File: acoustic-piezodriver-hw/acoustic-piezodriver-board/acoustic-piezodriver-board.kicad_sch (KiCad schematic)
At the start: 0 parts

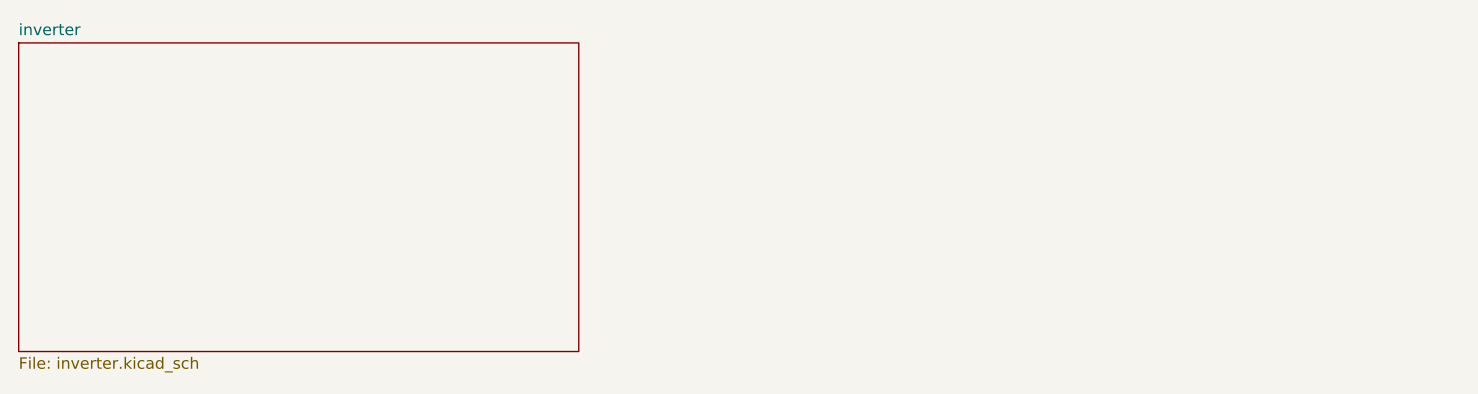
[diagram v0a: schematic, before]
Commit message: [carrier] Same as previous [piezodriver] Moved inverter to separate board
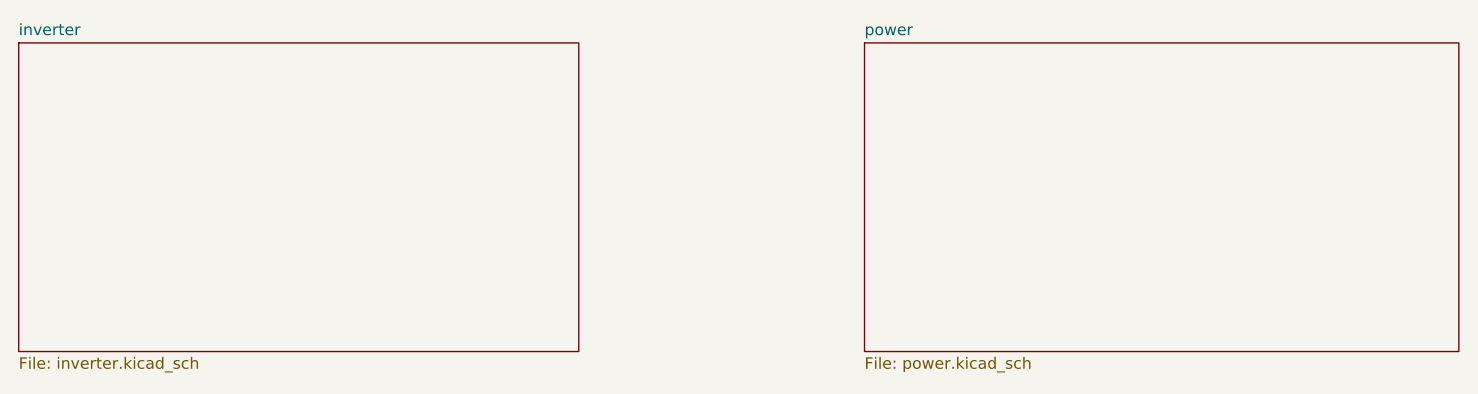
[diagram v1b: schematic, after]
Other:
- added sheet power (power.kicad_sch)
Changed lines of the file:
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@@
+		)
+	)
+	(sheet
+		(at 129.54 41.91)
+		(size 66.04 34.29)
+		(exclude_from_sim no)
+		(in_bom yes)
+		(on_board yes)
+		(dnp no)
+		(fields_autoplaced yes)
+		(stroke
+			(width 0.1524)
+			(type solid)
+		)
+		(fill
+			(color 0 0 0 0.0000)
+		)
+		(property "Sheetname" "power"
+			(at 129.54 41.1984 0)
+			(effects
+				(font
+					(size 1.27 1.27)
+				)
+				(justify left bottom)
+			)
+		)
+		(property "Sheetfile" "power.kicad_sch"
+			(at 129.54 76.7846 0)
+			(effects
+				(font
+					(size 1.27 1.27)
+				)
+				(justify left top)
+			)
+		)
+		(instances
+			(project "acoustic-piezodriver-board"
+				(path "/94cb090f-214e-44cc-b8ed-ae50ff29d2bf"
+					(page "3")
+				)
+			)
 		)
 	)
